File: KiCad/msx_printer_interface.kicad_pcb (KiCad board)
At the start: 2 copper layers, 65.5 x 54 mm, 9 parts, among them J1 MSX Cartridge Connector, J2 Conn_02x07_Top_Bottom, U1 ATF22V10C-15PU, U2 74HC273

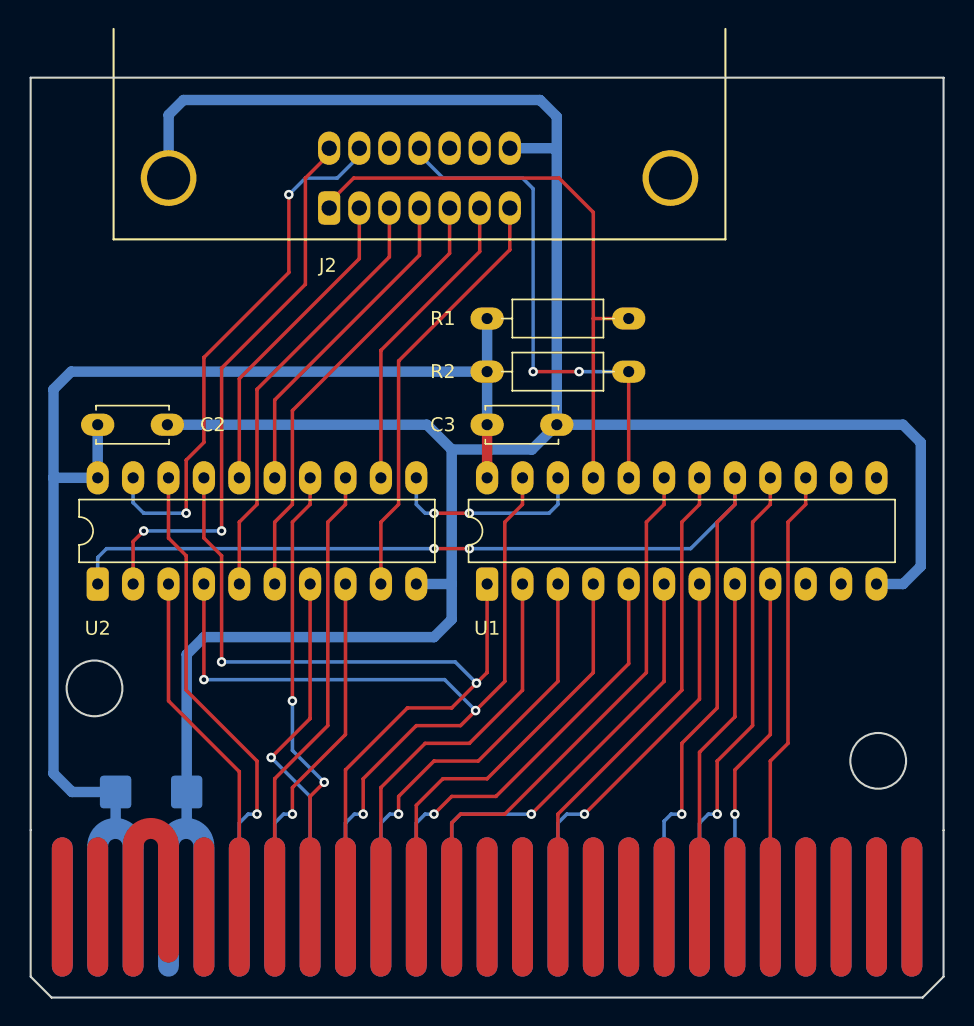
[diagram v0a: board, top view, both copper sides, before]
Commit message: Edge connector width adjusted to spec
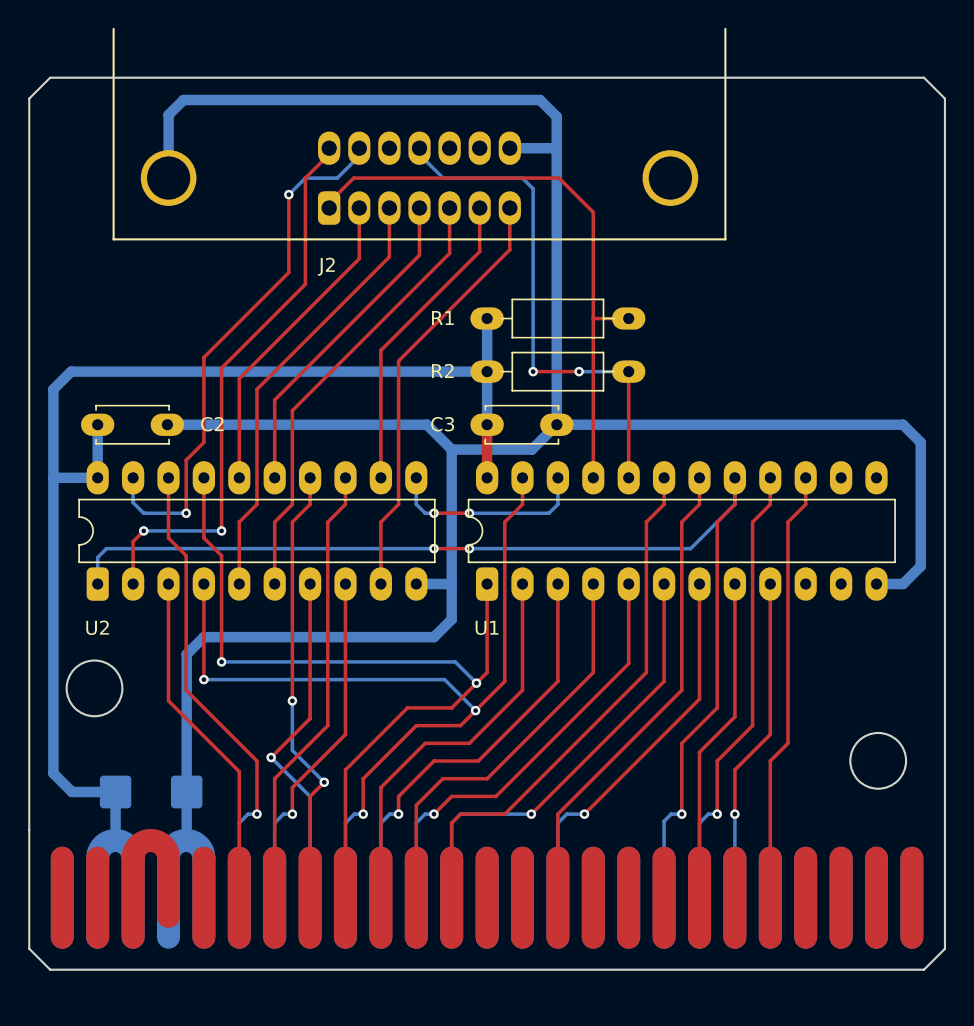
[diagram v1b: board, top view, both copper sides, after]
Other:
- board size 65.5 x 54 mm -> 65.7 x 54 mm

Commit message: Move C1
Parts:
- C1: moved to F.Cu
- R1, R2: value R_Small -> 5.6KΩ
- moved C1 30.2 mm to (33.9, 24.6)
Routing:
- net GND: track 175.1 -> 178.8 mm
- net VCC: track 85.5 -> 88.7 mm
- net CLK_DATA: vias 2 -> 1

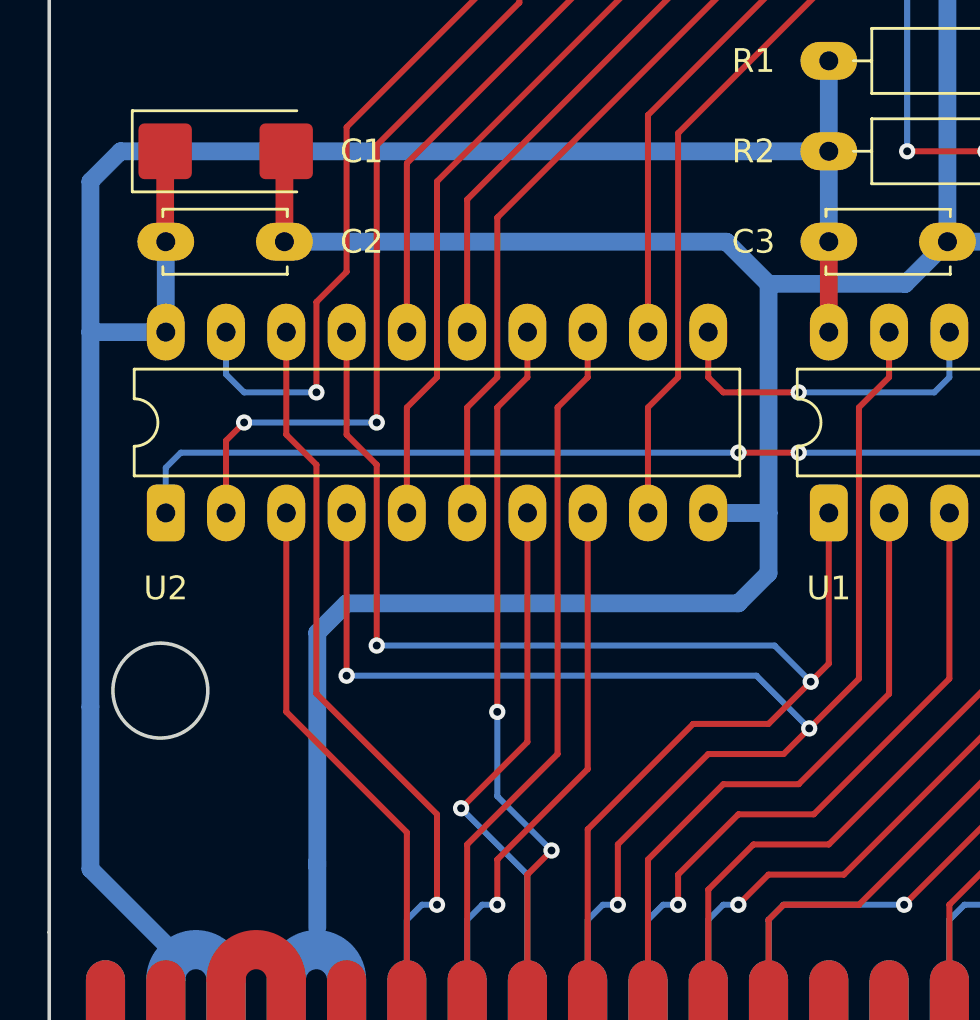
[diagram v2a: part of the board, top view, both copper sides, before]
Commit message: Change C1 value, routing
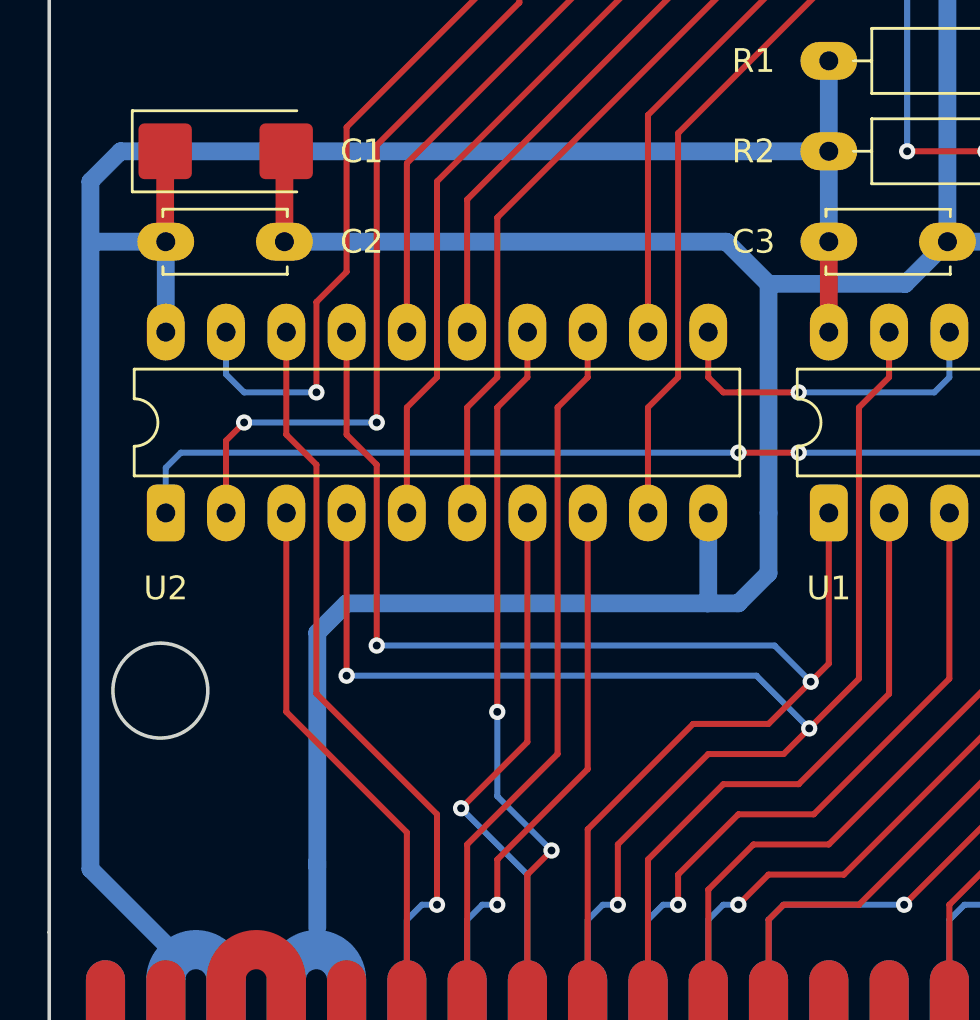
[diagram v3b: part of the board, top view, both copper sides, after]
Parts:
- C1: value 10uF -> 47uF
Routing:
- net GND: track 178.8 -> 180.1 mm
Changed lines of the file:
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@@
 			)
 		)
-		(property "Value" "10uF"
+		(property "Value" "47uF"
 			(at 0 2.55 0)
 			(layer "F.Fab")
@@
 			)
 		)
-		(property "DigiKey" "https://www.digikey.com/en/products/detail/kyocera-avx/TAJC106M016RNJ/563807"
+		(property "DigiKey" "https://www.digikey.com/en/products/detail/kyocera-avx/TAJC476K016RNJ/563823"
 			(at 0 0 0)
 			(unlocked yes)
@@
 			)
 		)
-		(property "Description" "Generic connector, double row, 02x25, odd/even pin numbering scheme (row 1 odd numbers, row 2 even numbers), script generated (kicad-library-utils/schlib/autogen/connector/)"
+		(property "Description" ""
 			(at 59.35 67.81175 0)
 			(layer "F.Fab")
@@
 		(fp_circle
 			(center 8.5 52)
-			(end 12.2 52)
+			(end 12 52)
 			(stroke
 				(width 0.15)
@@
 		)
 		(group ""
-			(members "33e19c18-9fde-41d6-a837-3ac6f410ecf5" "421ea485-ebdd-4447-85a1-197afe3d97f4"
-				"4f3aab66-7786-4dda-8edf-c5cfa3d5092e" "5aa466b8-e1f7-4127-b594-d000b68e6f8f"
-				"5df4519a-c737-44de-bd52-8d5b83c9cb71" "920a0756-aaba-4429-b604-1d7d423c4671"
-				"9b68a9f4-519d-4de1-9fd8-b4f6611dc923" "fa5141dd-2126-4877-a71b-819403615aa7"
+			(members "0d1cb053-31b3-4a4c-91ba-cbc5b1766db5" "1f14457b-bc11-43c4-bd6e-5eff9ca206e2"
+				"3ffb713f-a82c-4752-89be-6d3d8ca7c46d" "5fc785db-62cf-419f-adae-beceac25d76c"
+				"92d62f52-8fa7-422b-b3ba-6cd4ade9d95c" "a630b34a-fe61-4d41-b54e-8072f3b3b911"
 			)
 		)
 		(group ""
-			(members "23561fdc-64bd-4769-ab4a-f8823dbfd91e" "406a9515-ccdd-4836-918e-31e645d1dbb3"
-				"70f7a47d-5b4b-48cd-adc8-369b29695e2b" "bf3ffda9-7489-4698-8759-d52691954833"
-				"d6af21ee-93f9-4adc-b975-7fde04cc1972" "e2104778-4bf3-4b60-9d59-ee7268b6fbad"
+			(members "0305204f-423b-426b-bc97-b7d79ad7626a" "3c197ca5-9756-47e1-86d1-afbd8ae6f4f9"
+				"63f827d4-4ac1-4284-8c2f-ac0c86527fbc" "81a61776-bd45-4d46-a79e-ef28b8687b67"
+				"96ed02c3-bd62-4e66-9c78-2a23d4bb1f42" "a04f5c30-fcf9-4f2c-922a-938ce5ed9a54"
+				"b2c666bd-5b79-4bd9-ad35-c36587b96817" "f9f040fa-d694-4dee-a45d-53eb60bfe76f"
 			)
 		)
 		(group ""
-			(members "4c3c275a-6100-4732-90c0-d0799da6766a" "5826e602-0558-46df-a197-eb6a1ecfe1e4"
-				"83b74fc1-a9ef-4cd7-a6c6-cf8adbca7665" "8d44eff9-51c3-43f5-b690-1e9970c4acfe"
-				"99a1ad8a-d75b-404c-8a00-704ad932c5cb" "b28c4455-d424-48b8-ab3b-856e7ae03ff1"
+			(members "0af81e24-9bd0-467e-b640-251522c8f7df" "1b5fc8ef-30cd-4775-b6f9-f25ac34fa888"
+				"3c747ed8-bf5c-436a-bc1a-aa853afdb350" "424fa3ea-59e5-46ce-9c62-e5ca5cbbf8c8"
+				"6e910987-dff1-47df-a7b9-7a0a849e9a8d" "8cab6eb0-2e4a-424e-ac94-9692439c04ab"
+				"9035bd0d-06e0-4b69-b725-e24205395477" "a93775a2-de59-48b0-905f-0861cbc40126"
 			)
 		)
 		(group ""
-			(members "01a9c609-b23f-42d4-ad3c-509c69168fc0" "20d3637b-9d70-4c17-a777-401c8173e88c"
-				"6dcdb4aa-a013-4eda-937e-b30660525c41" "917266ca-d323-4a32-a6c2-b0e70ce255ad"
-				"b07268e0-dd7b-4bb2-9a88-c3cbdfc6f3bc" "c2922b93-3edc-4f1c-a852-258f37ebd2ae"
-				"c787b43d-2bbd-47fe-94bc-1f0da81241d4" "cbd9edf6-c36b-411e-a990-000e69b35935"
+			(members "21c1b483-9a5c-4508-8723-58963016b745" "3f39fc18-f36c-4dba-a450-dcc60e34c7b1"
+				"84acffe4-17a9-4625-bb48-93741fcfba11" "85fc2f47-e719-431d-98a9-4e8405842b20"
+				"bfb67930-f025-44ba-a1c0-18ed7de282a4" "e94cd92c-ae76-4cc4-a457-f189bedf6eb9"
 			)
 		)
@@
 	)
 	(segment
-		(start 31.385 28.375)
-		(end 31.41 28.4)
+		(start 59.35 28.4)
+		(end 59.35 32.21)
 		(width 0.75)
 		(layer "F.Cu")
@@
 	)
 	(segment
-		(start 59.35 28.4)
-		(end 59.35 32.21)
+		(start 31.385 24.59)
+		(end 31.385 28.375)
 		(width 0.75)
 		(layer "F.Cu")
@@
 	)
 	(segment
-		(start 31.385 24.59)
-		(end 31.385 28.375)
-		(width 0.75)
-		(layer "F.Cu")
+		(start 29.505 24.59)
+		(end 28.235 25.86)
+		(width 0.75)
+		(layer "B.Cu")
 		(net 1)
 	)
 	(segment
-		(start 31.41 32.21)
-		(end 28.235 32.21)
+		(start 28.235 54.835)
+		(end 31.63 58.23)
 		(width 0.75)
 		(layer "B.Cu")
@@
 	)
 	(segment
+		(start 31.41 28.4)
+		(end 28.485 28.4)
+		(width 0.75)
+		(layer "B.Cu")
+		(net 1)
+	)
+	(segment
+		(start 59.35 24.59)
+		(end 59.35 28.4)
+		(width 0.75)
+		(layer "B.Cu")
+		(net 1)
+	)
+	(segment
 		(start 28.235 25.86)
-		(end 29.505 24.59)
+		(end 28.235 54.835)
 		(width 0.75)
 		(layer "B.Cu")
@@
 	(segment
 		(start 59.35 24.59)
-		(end 59.35 28.4)
-		(width 0.75)
-		(layer "B.Cu")
-		(net 1)
-	)
-	(segment
-		(start 28.235 32.21)
-		(end 28.235 25.86)
-		(width 0.75)
-		(layer "B.Cu")
-		(net 1)
-	)
-	(segment
-		(start 29.505 24.59)
-		(end 59.35 24.59)
-		(width 0.75)
-		(layer "B.Cu")
-		(net 1)
-	)
-	(segment
-		(start 28.235 32.21)
-		(end 28.235 48)
-		(width 0.75)
-		(layer "B.Cu")
-		(net 1)
-	)
-	(segment
-		(start 28.235 54.835)
-		(end 31.63 58.23)
+		(end 29.505 24.59)
 		(width 0.75)
 		(layer "B.Cu")
@@
 	)
 	(segment
-		(start 28.235 48)
-		(end 28.235 54.835)
-		(width 0.75)
-		(layer "B.Cu")
-		(net 1)
-	)
-	(segment
 		(start 31.41 28.4)
 		(end 31.41 32.21)
@@
 		(width 0.75)
 		(layer "F.Cu")
+		(net 2)
+	)
+	(segment
+		(start 54.25 43.64)
+		(end 55.54 43.64)
+		(width 0.75)
+		(layer "B.Cu")
 		(net 2)
 	)
@@
 	)
 	(segment
+		(start 54.27 39.83)
+		(end 54.27 43.62)
+		(width 0.75)
+		(layer "B.Cu")
+		(net 2)
+	)
+	(segment
 		(start 90.465 29.67)
 		(end 90.465 38.56)
@@
 	(segment
 		(start 39.03 43.64)
-		(end 55.54 43.64)
+		(end 54.25 43.64)
 		(width 0.75)
 		(layer "B.Cu")
@@
 	)
 	(segment
+		(start 54.27 43.62)
+		(end 54.25 43.64)
+		(width 0.75)
+		(layer "B.Cu")
+		(net 2)
+	)
+	(segment
 		(start 62.572 30.178)
 		(end 64.35 28.4)
@@
 		(width 0.75)
 		(layer "B.Cu")
-		(net 2)
-	)
-	(segment
-		(start 54.27 39.83)
-		(end 56.81 39.83)
-		(width 0.75)
-		(layer "B.Cu")

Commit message: Silkscreen
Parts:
- added G***: LOGO, msx_printer_interface:msx_logo, F.Cu at (84.2, 7.60)
- added G***: LOGO, msx_printer_interface:bipyramid, F.Cu at (78.2, 20.9)
- added G***: LOGO, msx_printer_interface:tangent, B.Cu at (81.0, 19.1)
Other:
- board text added: "MSX Printer Interface ◆ Rev. 0 ◆ tangent.space 2025"
